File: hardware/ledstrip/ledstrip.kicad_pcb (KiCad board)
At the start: 4 copper layers, 107 x 107.5 mm, 117 parts, among them J1 Conn_ARM_JTAG_SWD_10, J2 USB_C_Receptacle_USB2.0_16P, J4 BMS connectors, J5 Ledstrip connector, J6 Header for STUSB4500 I2C, Q1 Q_NMOS, Q10 Q_PMOS, Q11 Q_NMOS, Q2 Q_NMOS, Q3 Q_NMOS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

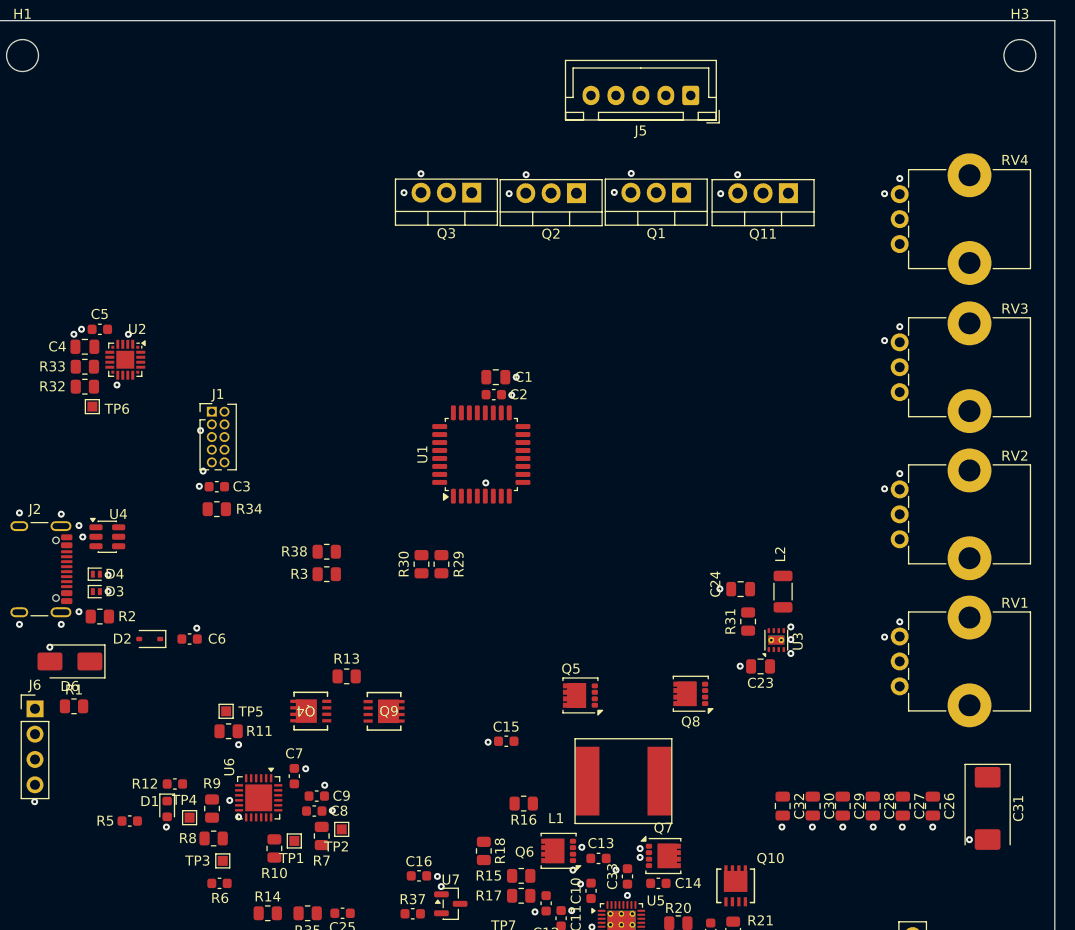
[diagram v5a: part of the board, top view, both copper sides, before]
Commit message: Add 3.3V and 12V zones on L3, add vias.
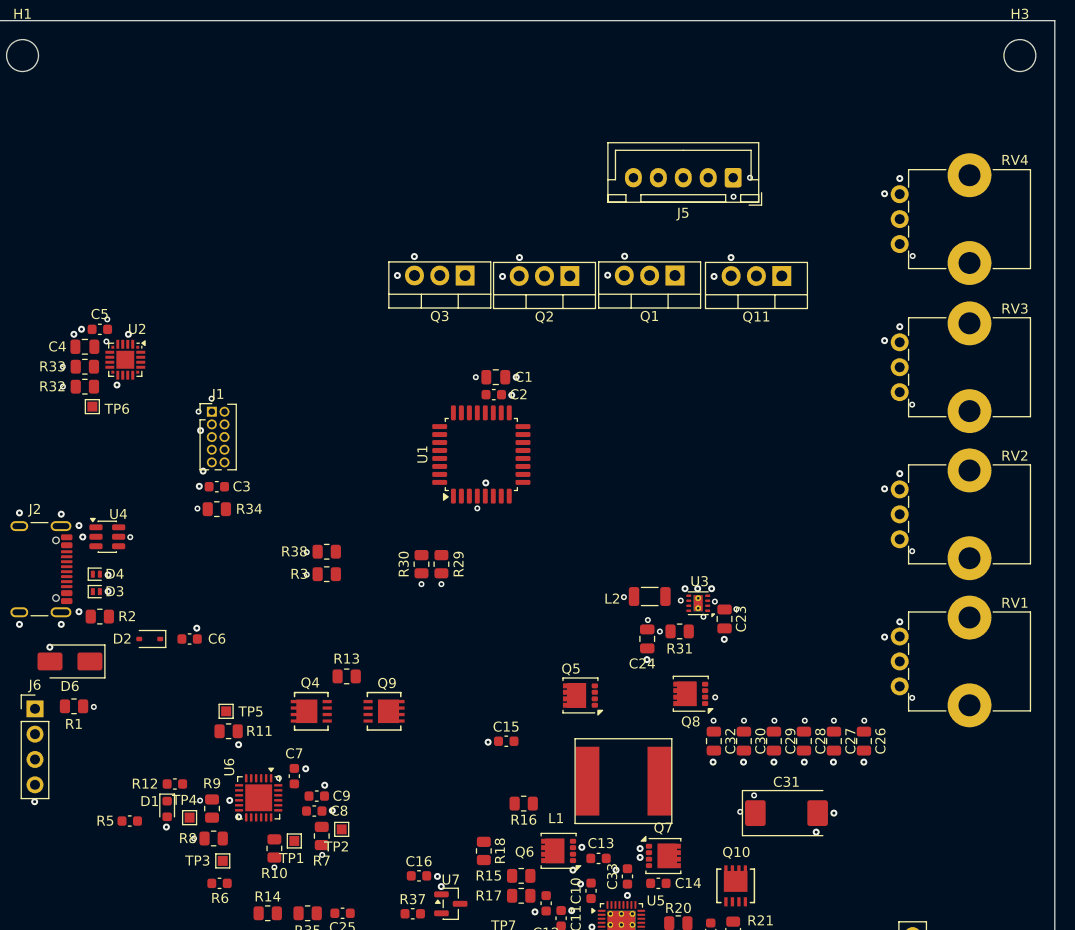
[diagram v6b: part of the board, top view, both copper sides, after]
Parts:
- moved C31 20.2 mm to (176.3, 124.2), turned to 0 degrees
- moved L2 13.4 mm to (162.6, 102.5), turned to 180 degrees
- moved C24 10.6 mm to (162.4, 106.7), turned to -90 degrees
- moved C26 9.49 mm to (184.1, 117.0)
- moved C27 9.49 mm to (181.1, 117.0)
- moved C28 9.49 mm to (178.1, 117.0)
- moved C29 9.49 mm to (175.1, 117.0)
- moved C30 9.49 mm to (172.1, 117.0)
- moved C32 9.49 mm to (169.1, 117.0)
- moved J5 9.28 mm to (171.0, 60.5)
- moved U3 8.66 mm to (167.5, 103.2), turned to 180 degrees
- moved Q1 8.33 mm to (165.2, 70.3)
- moved Q11 8.33 mm to (175.9, 70.4)
- moved Q2 8.33 mm to (154.6, 70.4)
- moved Q3 8.33 mm to (144.1, 70.3)
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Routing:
- net GND: vias 81 -> 83
- net +3.3V: vias 0 -> 28
- net +12V: vias 0 -> 13
- added copper zone on In2.Cu, net +12V
- added copper zone on In2.Cu, net +3.3V

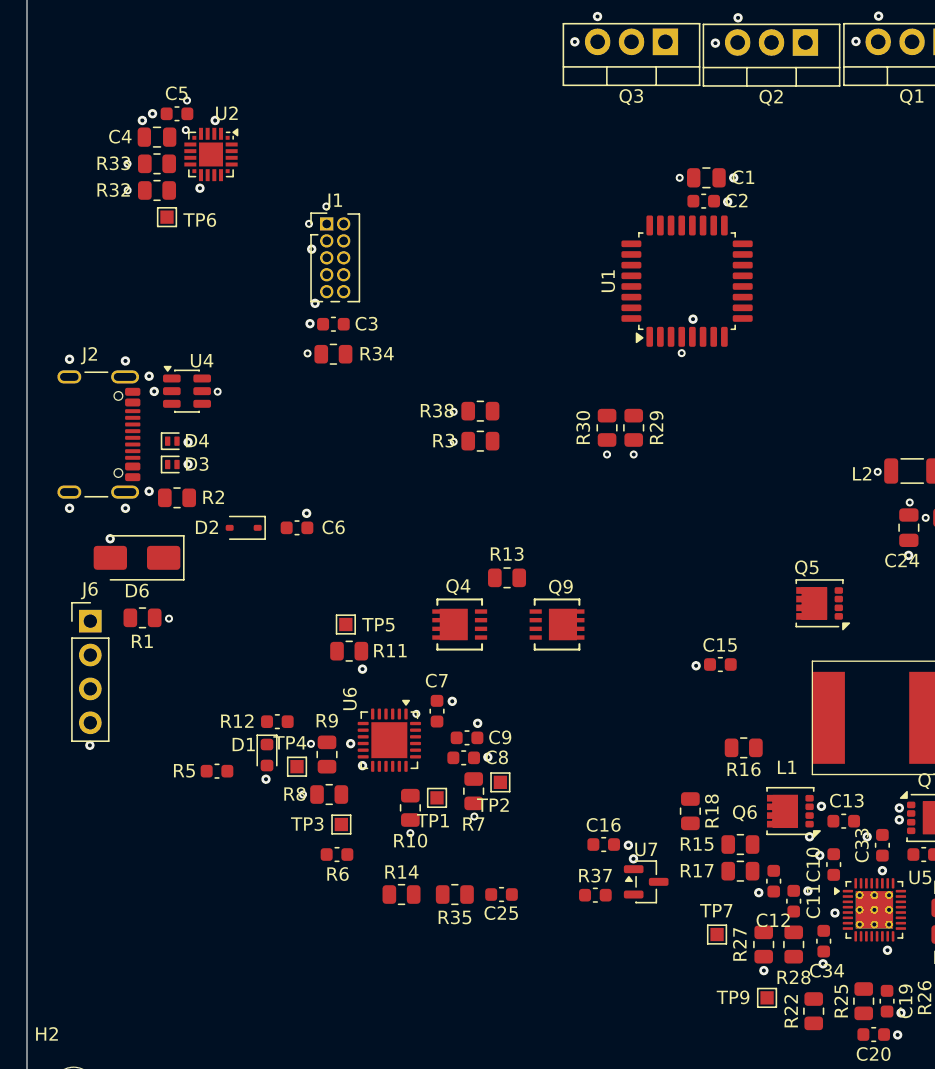
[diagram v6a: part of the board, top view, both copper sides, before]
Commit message: Start editing some trace.
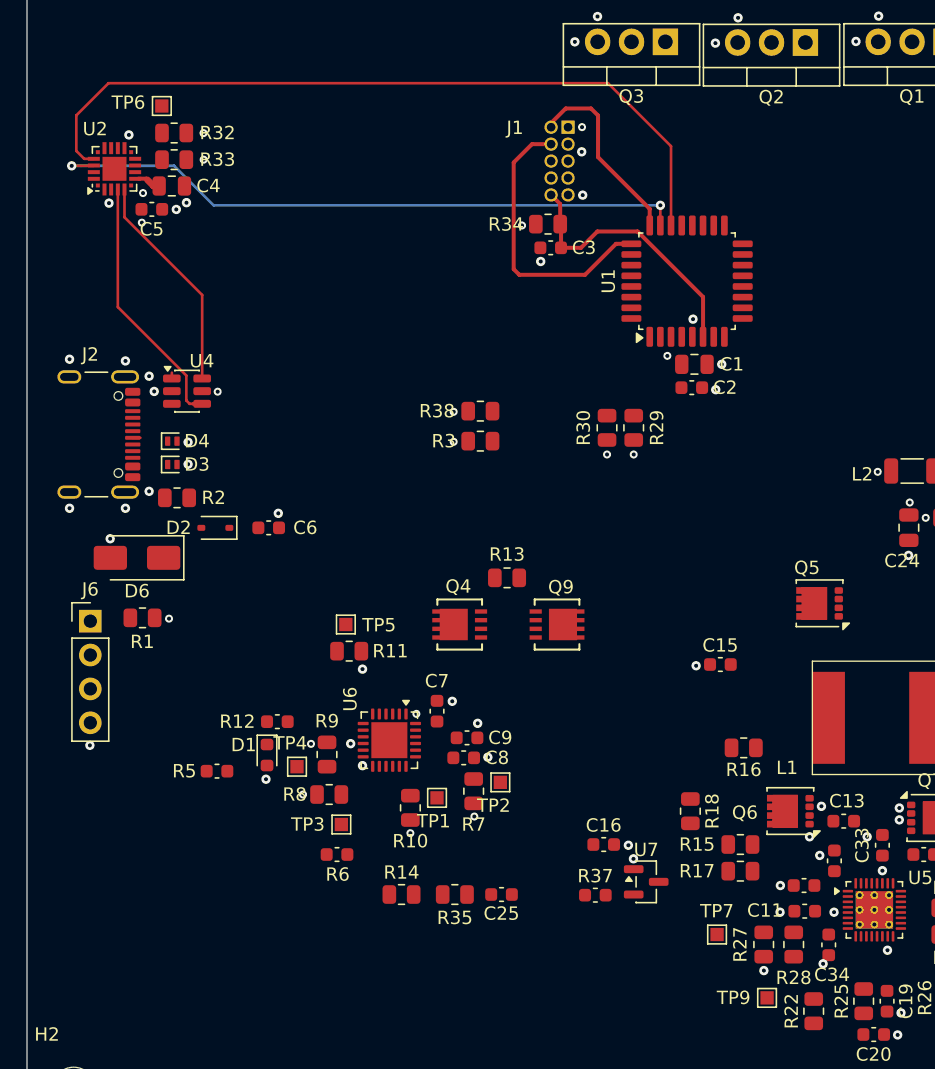
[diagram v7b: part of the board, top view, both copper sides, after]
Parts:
- J1: moved to B.Cu
- moved J1 19.5 mm to (136.8, 76.7), turned to 180 degrees
- moved R34 18.8 mm to (135.3, 84.0)
- moved C3 17.3 mm to (135.5, 85.8)
- moved C1 14.0 mm to (146.3, 94.5)
- moved C2 14.0 mm to (146.1, 96.2)
- moved TP6 8.35 mm to (106.4, 75.1), turned to 180 degrees
- moved C5 7.41 mm to (105.6, 82.9), turned to 0 degrees
- moved U2 7.32 mm to (102.8, 79.8), turned to 90 degrees
- moved R32 4.50 mm to (107.3, 77.1), turned to 0 degrees
- moved C4 3.83 mm to (107.1, 81.1), turned to 0 degrees
- moved C12 2.30 mm to (154.5, 133.6), turned to 0 degrees
- moved C6 2.12 mm to (114.4, 106.8)
- moved D2 2.12 mm to (110.4, 106.8)
- moved R33 1.32 mm to (107.3, 79.1), turned to 0 degrees
- moved C11 1.11 mm to (154.6, 135.5), turned to 0 degrees
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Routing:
- net /CP2102N_RXD: track 0.00 -> 57.7 mm
- net /CP2102N_TXD: track 0.00 -> 48.6 mm, vias 0 -> 2
- net /DBG_SWDCLK: track 0.00 -> 21.3 mm
- net /DBG_RESET: track 0.00 -> 20.5 mm
- net /CP2102N_D+: track 0.00 -> 19.2 mm
- net /CP2102N_D-: track 0.00 -> 16.6 mm
- net /DBG_SWDIO: track 0.00 -> 14.4 mm
- net +3.3V: track 0.00 -> 1.78 mm, vias 28 -> 26
- net /USB_D-: track 0.00 -> 1.01 mm

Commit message: All signal tracks done, PCB almost terminated
Only GND, 3.3V and 12V pins-to-via tracks left.
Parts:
- moved C25 17.4 mm to (138.5, 118.2)
- moved R35 17.4 mm to (135.0, 118.2)
- moved R14 16.6 mm to (134.9, 121.5)
- moved R32 15.5 mm to (122.8, 77.2)
- moved R33 15.5 mm to (122.8, 79.2)
- moved U2 15.5 mm to (118.3, 79.8)
- moved C4 15.5 mm to (122.6, 81.1)
- moved C5 15.5 mm to (121.1, 82.9)
- moved TP6 15.5 mm to (121.9, 75.1)
- moved D6 10.1 mm to (110.4, 100.8), turned to 0 degrees
- moved D4 6.96 mm to (105.9, 93.4)
- moved R3 6.77 mm to (130.0, 93.5)
- moved R38 6.77 mm to (130.0, 91.2)
- moved D3 4.38 mm to (105.3, 106.0)
- moved C6 3.60 mm to (112.0, 109.5)
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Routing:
- net /Battery Charger/BQ25703A_SCL: track 0.00 -> 164.0 mm, vias 0 -> 3
- net /Battery Charger/BQ25703A_SDA: track 0.00 -> 152.5 mm, vias 0 -> 3
- net /Battery Charger/BQ25703A_PROCHOT: track 0.00 -> 79.4 mm, vias 0 -> 2
- net /Battery Charger/V_SNK: track 0.00 -> 56.6 mm, vias 0 -> 2
- net /Battery Charger/BQ25703A_CHRG_OK: track 0.00 -> 56.1 mm, vias 0 -> 2
- net /USB PD/USB_CC1: track 0.00 -> 52.4 mm, vias 0 -> 2
- net /Pots/POT_W: track 0.00 -> 51.4 mm
- net +12V: track 0.00 -> 47.5 mm
- net /Pots/POT_R: track 0.00 -> 47.3 mm
- net Net-(D2-A): track 0.00 -> 44.4 mm
- net /Pots/POT_B: track 0.00 -> 42.6 mm
- net BQ25703A_REGN: track 0.00 -> 42.2 mm, vias 0 -> 2
- net /USB PD/USB_CC2: track 0.00 -> 40.6 mm, vias 0 -> 2
- net /Pots/POT_G: track 0.00 -> 39.9 mm
- net /leds/PWM_W: track 0.00 -> 34.5 mm
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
